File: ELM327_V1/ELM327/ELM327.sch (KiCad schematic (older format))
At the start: 0 parts

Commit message: update to elm327 done missing esp32 missing GPS missing GSM
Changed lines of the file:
@@
 $EndDescr
 $Sheet
-S 3275 1050 2100 1575
+S 10000 625  1100 250
 U 61B559C8
 F0 "ELM327_IC" 50
 F1 "ELM327_IC.sch" 50
+F2 "ENABLE_PIN_LEVELSHIFTER" I L 10000 675 50
+F3 "ELM327_RX" B L 10000 750 50
+F4 "ELM327_TX" B L 10000 825 50
 $EndSheet
 $EndSCHEMATC

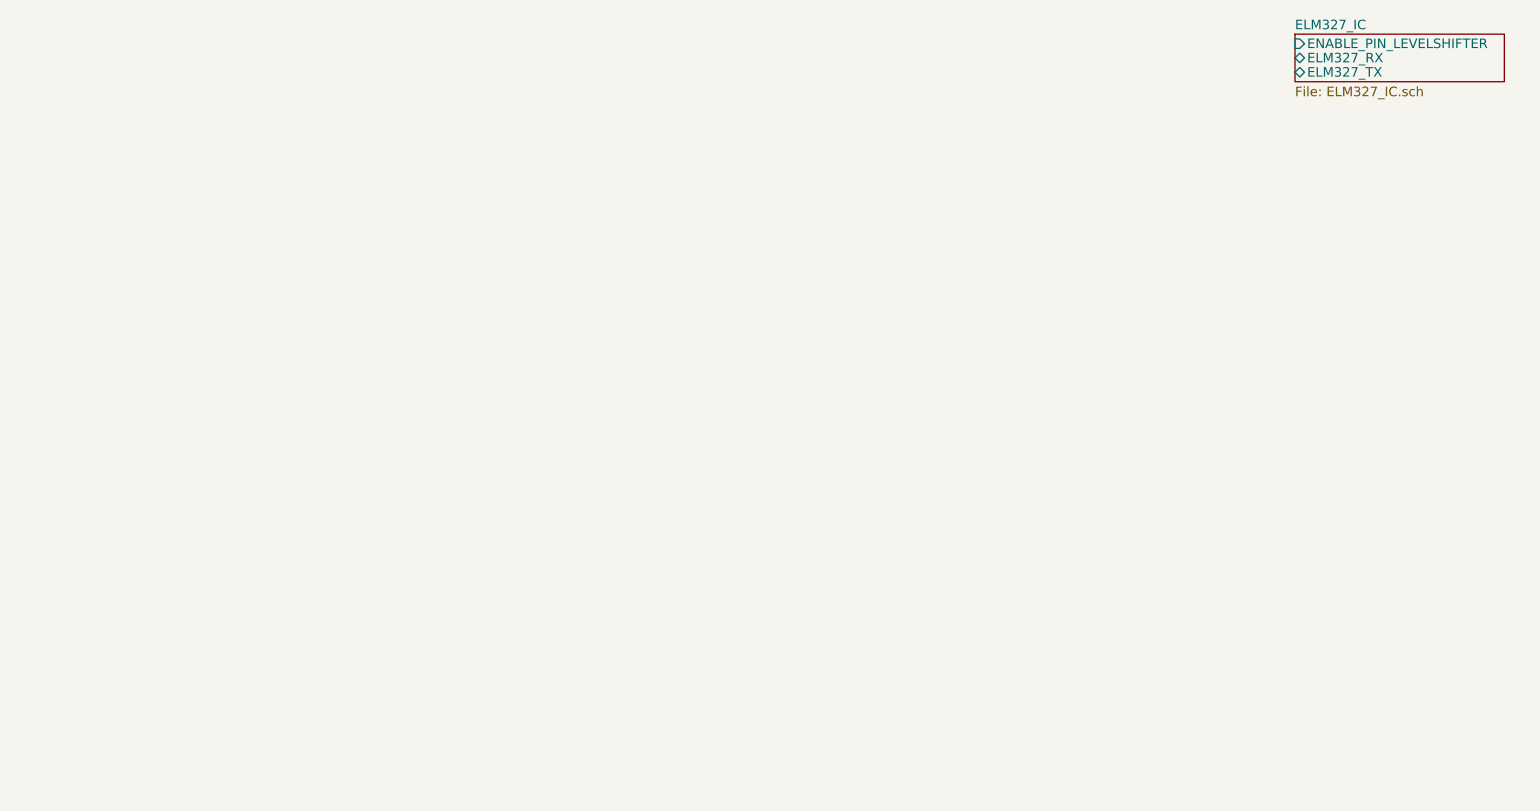
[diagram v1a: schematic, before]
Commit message: update to elm327 and data sheet
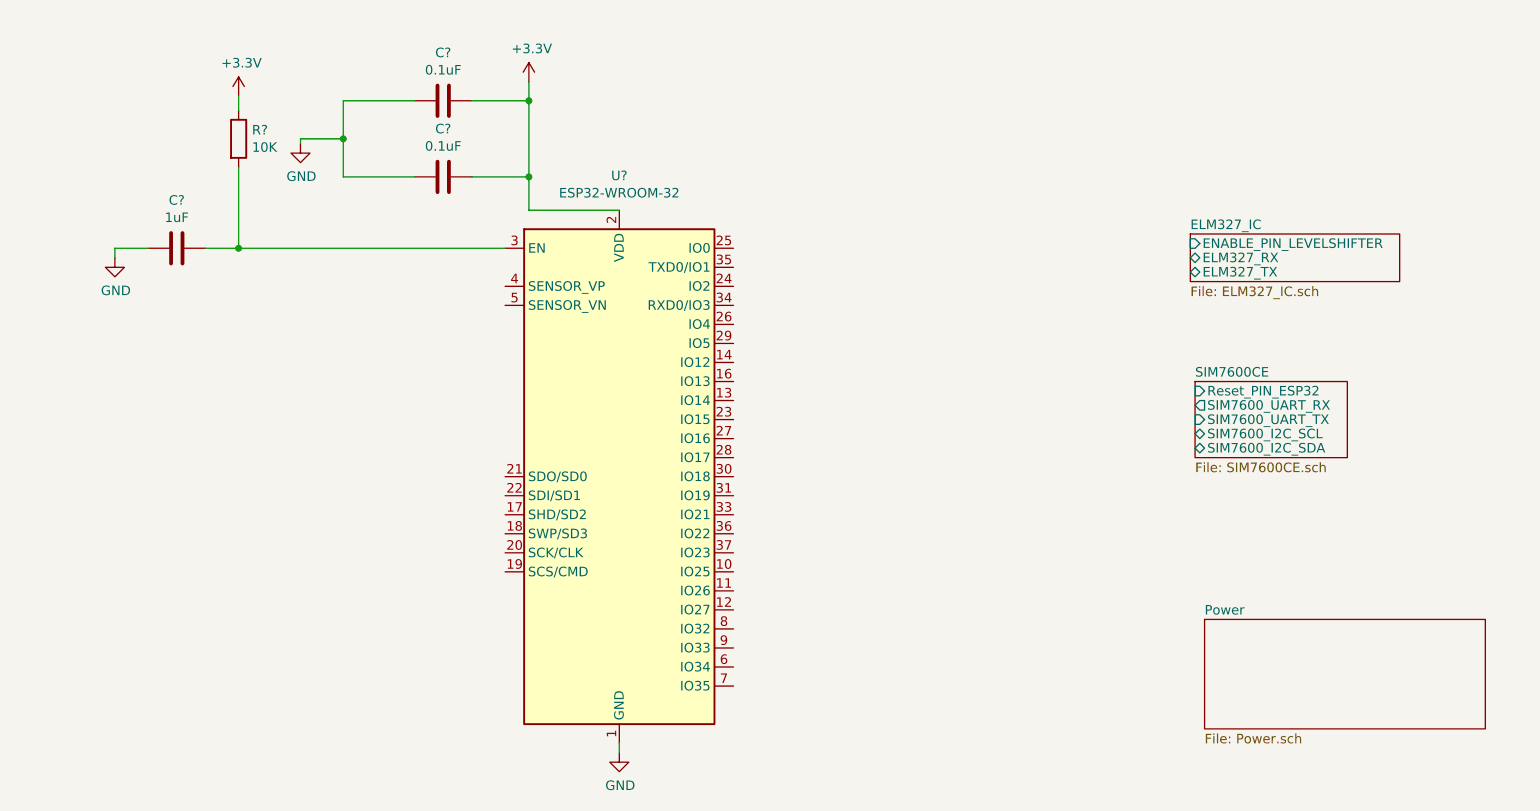
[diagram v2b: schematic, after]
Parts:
- added C? (x2): 0.1uF, symbol Device:C
- added C?: 1uF, symbol Device:C
- added R?: 10K, symbol Device:R
- added U?: ESP32-WROOM-32, RF_Module:ESP32-WROOM-32, symbol RF_Module:ESP32-WROOM-32
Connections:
- new net: C?.2, R?.2, U?.3 (EN)
- new net +3V3: C?.2, C?.2, R?.1, U?.2 (VDD)
- new net GND: C?.1, C?.1, C?.1, U?.1 (GND), U?.15 (GND), U?.38 (GND), U?.39 (GND)
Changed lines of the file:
@@
 $Descr A4 11693 8268
 encoding utf-8
-Sheet 1 2
+Sheet 1 4
 Title ""
 Date ""
@@
 $EndDescr
 $Sheet
-S 10000 625  1100 250
+S 9450 1675 1100 250
 U 61B559C8
 F0 "ELM327_IC" 50
 F1 "ELM327_IC.sch" 50
-F2 "ENABLE_PIN_LEVELSHIFTER" I L 10000 675 50
-F3 "ELM327_RX" B L 10000 750 50
-F4 "ELM327_TX" B L 10000 825 50
+F2 "ENABLE_PIN_LEVELSHIFTER" I L 9450 1725 50
+F3 "ELM327_RX" B L 9450 1800 50
+F4 "ELM327_TX" B L 9450 1875 50
+$EndSheet
+$Comp
+L RF_Module:ESP32-WROOM-32 U?
+U 1 1 61B78808
+P 6450 2950
+F 0 "U?" H 6450 4531 50  0000 C CNN
+F 1 "ESP32-WROOM-32" H 6450 4440 50  0000 C CNN
+F 2 "RF_Module:ESP32-WROOM-32" H 6450 1450 50  0001 C CNN
+F 3 "https://www.espressif.com/sites/default/files/documentation/esp32-wroom-32_datasheet_en.pdf" H 6150 3000 50  0001 C CNN
+	1    6450 2950
+	1    0    0    -1
+$EndComp
+$Comp
+L power:+3.3V #PWR?
+U 1 1 61B8CF39
+P 4450 950
+F 0 "#PWR?" H 4450 800 50  0001 C CNN
+F 1 "+3.3V" H 4465 1123 50  0000 C CNN
+F 2 "" H 4450 950 50  0001 C CNN
+F 3 "" H 4450 950 50  0001 C CNN
+	1    4450 950
+	1    0    0    -1
+$EndComp
+$Comp
+L power:+3.3V #PWR?
+U 1 1 61B8DD97
+P 5975 875
+F 0 "#PWR?" H 5975 725 50  0001 C CNN
+F 1 "+3.3V" H 5990 1048 50  0000 C CNN
+F 2 "" H 5975 875 50  0001 C CNN
+F 3 "" H 5975 875 50  0001 C CNN
+	1    5975 875
+	1    0    0    -1
+$EndComp
+Wire Wire Line
+	5975 1550 6450 1550
+$Comp
+L power:GND #PWR?
+U 1 1 61B8F0DF
+P 6450 4400
+F 0 "#PWR?" H 6450 4150 50  0001 C CNN
+F 1 "GND" H 6455 4227 50  0000 C CNN
+F 2 "" H 6450 4400 50  0001 C CNN
+F 3 "" H 6450 4400 50  0001 C CNN
+	1    6450 4400
+	1    0    0    -1
+$EndComp
+Wire Wire Line
+	6450 4400 6450 4350
+$Comp
+L Device:C C?
+U 1 1 61B9108D
+P 5525 1375
+F 0 "C?" V 5777 1375 50  0000 C CNN
+F 1 "0.1uF" V 5686 1375 50  0000 C CNN
+F 2 "" H 5563 1225 50  0001 C CNN
+F 3 "~" H 5525 1375 50  0001 C CNN
+	1    5525 1375
+	0    -1   -1   0
+$EndComp
+$Comp
+L Device:C C?
+U 1 1 61B91E1D
+P 5525 975
+F 0 "C?" V 5777 975 50  0000 C CNN
+F 1 "0.1uF" V 5686 975 50  0000 C CNN
+F 2 "" H 5563 825 50  0001 C CNN
+F 3 "~" H 5525 975 50  0001 C CNN
+	1    5525 975
+	0    -1   -1   0
+$EndComp
+Wire Wire Line
+	5975 875  5975 975
+Wire Wire Line
+	5975 975  5675 975
+Wire Wire Line
+	5675 1375 5975 1375
+Wire Wire Line
+	5975 1375 5975 1550
+Wire Wire Line
+	5975 1375 5975 975
+Connection ~ 5975 1375
+Connection ~ 5975 975
+Wire Wire Line
+	5375 1375 5000 1375
+Wire Wire Line
+	5000 1375 5000 1175
+Wire Wire Line
+	5000 975  5375 975
+$Comp
+L power:GND #PWR?
+U 1 1 61B9CE7F
+P 4775 1200
+F 0 "#PWR?" H 4775 950 50  0001 C CNN
+F 1 "GND" H 4780 1027 50  0000 C CNN
+F 2 "" H 4775 1200 50  0001 C CNN
+F 3 "" H 4775 1200 50  0001 C CNN
+	1    4775 1200
+	1    0    0    -1
+$EndComp
+Wire Wire Line
+	5000 1175 4775 1175
+Wire Wire Line
+	4775 1175 4775 1200
+Connection ~ 5000 1175
+Wire Wire Line
+	5000 1175 5000 975
+$Comp
+L Device:R R?
+U 1 1 61BA0A50
+P 4450 1175
+F 0 "R?" H 4520 1221 50  0000 L CNN
+F 1 "10K" H 4520 1130 50  0000 L CNN
+F 2 "" V 4380 1175 50  0001 C CNN
+F 3 "~" H 4450 1175 50  0001 C CNN
+	1    4450 1175
+	1    0    0    -1
+$EndComp
+Wire Wire Line
+	4450 1025 4450 950
+Wire Wire Line
+	4450 1325 4450 1750
+Wire Wire Line
+	4450 1750 5850 1750
+$Comp
+L Device:C C?
+U 1 1 61BA1834
+P 4125 1750
+F 0 "C?" V 4377 1750 50  0000 C CNN
+F 1 "1uF" V 4286 1750 50  0000 C CNN
+F 2 "" H 4163 1600 50  0001 C CNN
+F 3 "~" H 4125 1750 50  0001 C CNN
+	1    4125 1750
+	0    -1   -1   0
+$EndComp
+Wire Wire Line
+	4275 1750 4450 1750
+Connection ~ 4450 1750
+$Comp
+L power:GND #PWR?
+U 1 1 61BA1F72
+P 3800 1800
+F 0 "#PWR?" H 3800 1550 50  0001 C CNN
+F 1 "GND" H 3805 1627 50  0000 C CNN
+F 2 "" H 3800 1800 50  0001 C CNN
+F 3 "" H 3800 1800 50  0001 C CNN
+	1    3800 1800
+	1    0    0    -1
+$EndComp
+Wire Wire Line
+	3975 1750 3800 1750
+Wire Wire Line
+	3800 1750 3800 1800
+$Sheet
+S 9475 2450 800  400
+U 61BA48F5
+F0 "SIM7600CE" 50
+F1 "SIM7600CE.sch" 50
+F2 "Reset_PIN_ESP32" I L 9475 2500 50
+F3 "SIM7600_UART_RX" O L 9475 2575 50
+F4 "SIM7600_UART_TX" I L 9475 2650 50
+F5 "SIM7600_I2C_SCL" B L 9475 2725 50
+F6 "SIM7600_I2C_SDA" B L 9475 2800 50
+$EndSheet
+$Sheet
+S 9525 3700 1475 575
+U 61DE7DB3
+F0 "Power" 50
+F1 "Power.sch" 50
 $EndSheet
 $EndSCHEMATC
